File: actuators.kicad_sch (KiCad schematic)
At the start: 23 parts, among them U2 DRV8871 H-мост, U3 DRV8871 H-мост, U4 DRV8871 H-мост, U5 DRV8871 H-мост

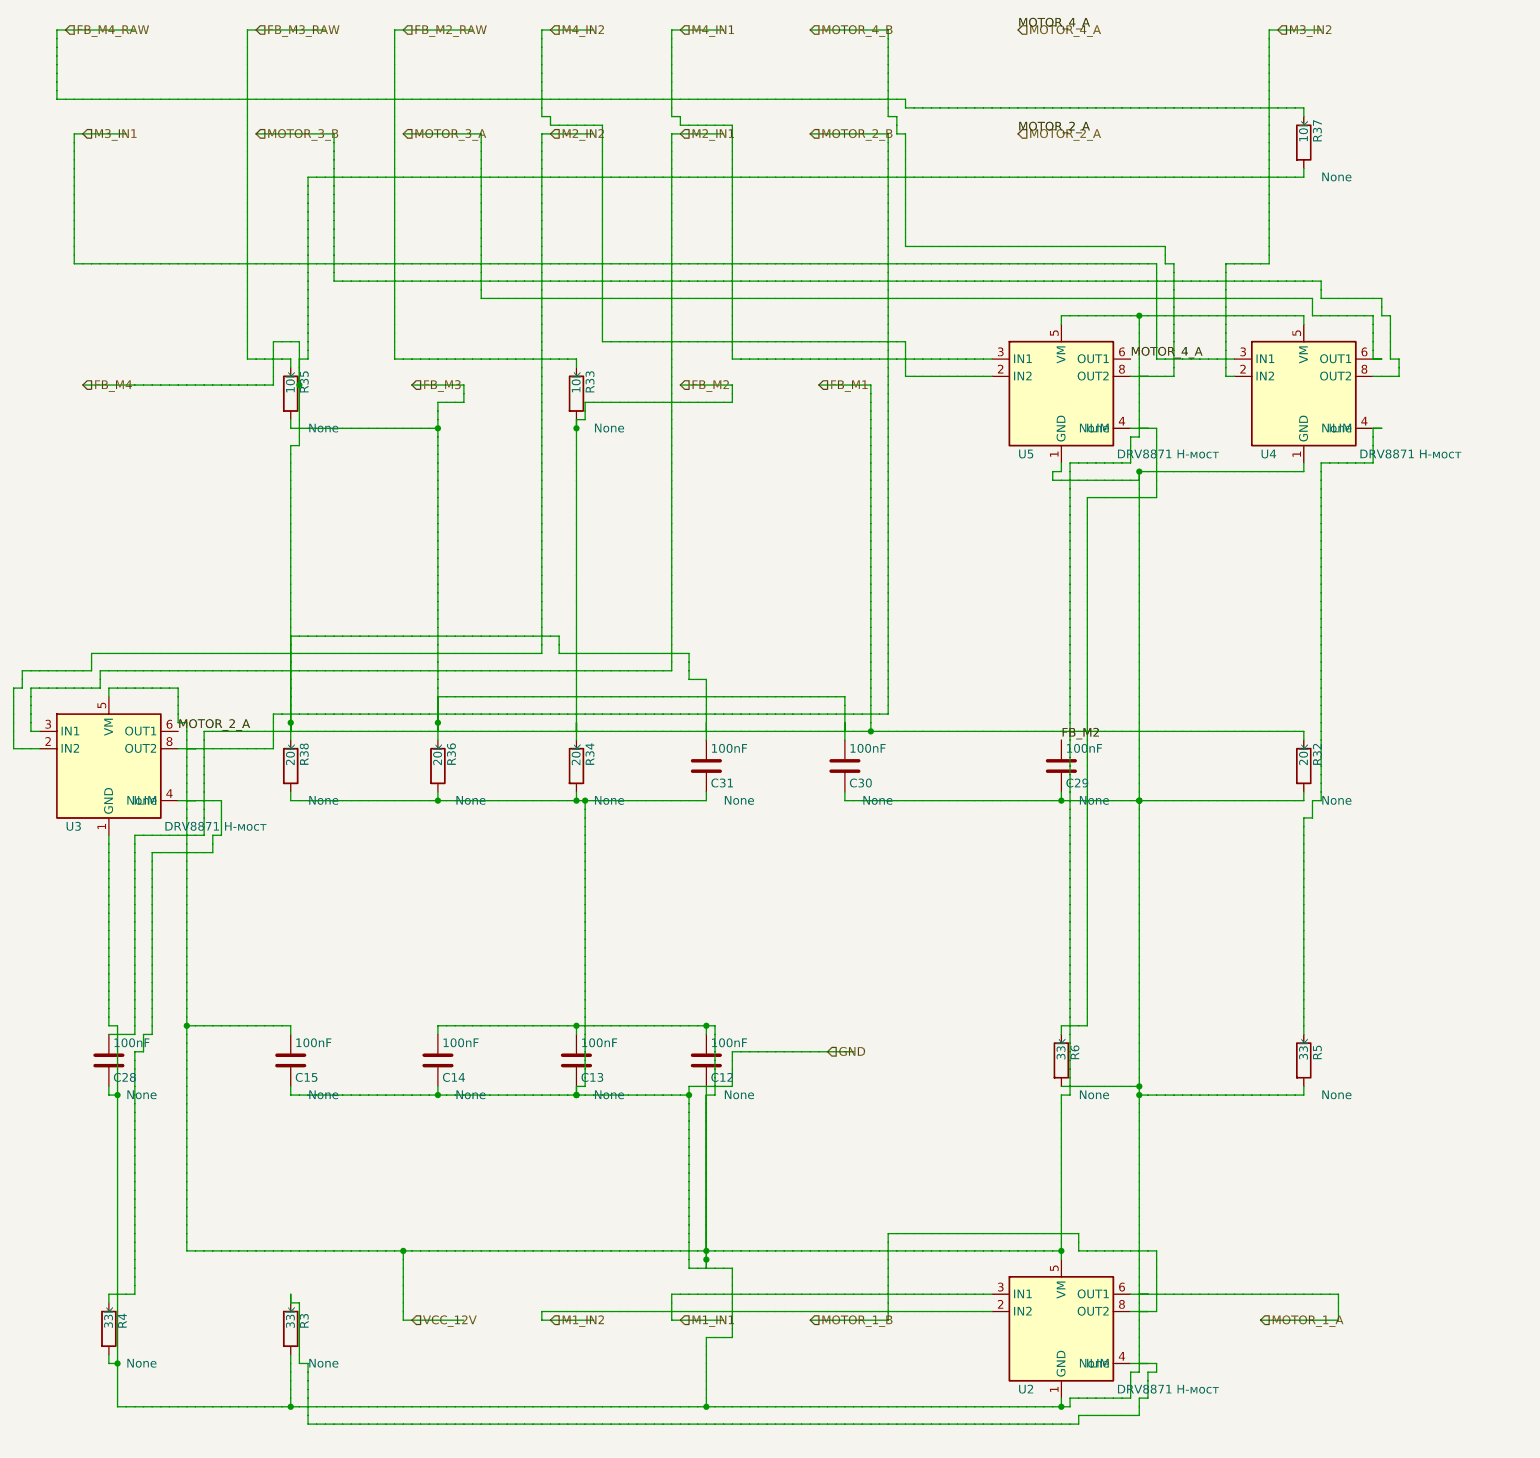
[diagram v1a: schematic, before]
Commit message: fix router map cell no more mark for pins
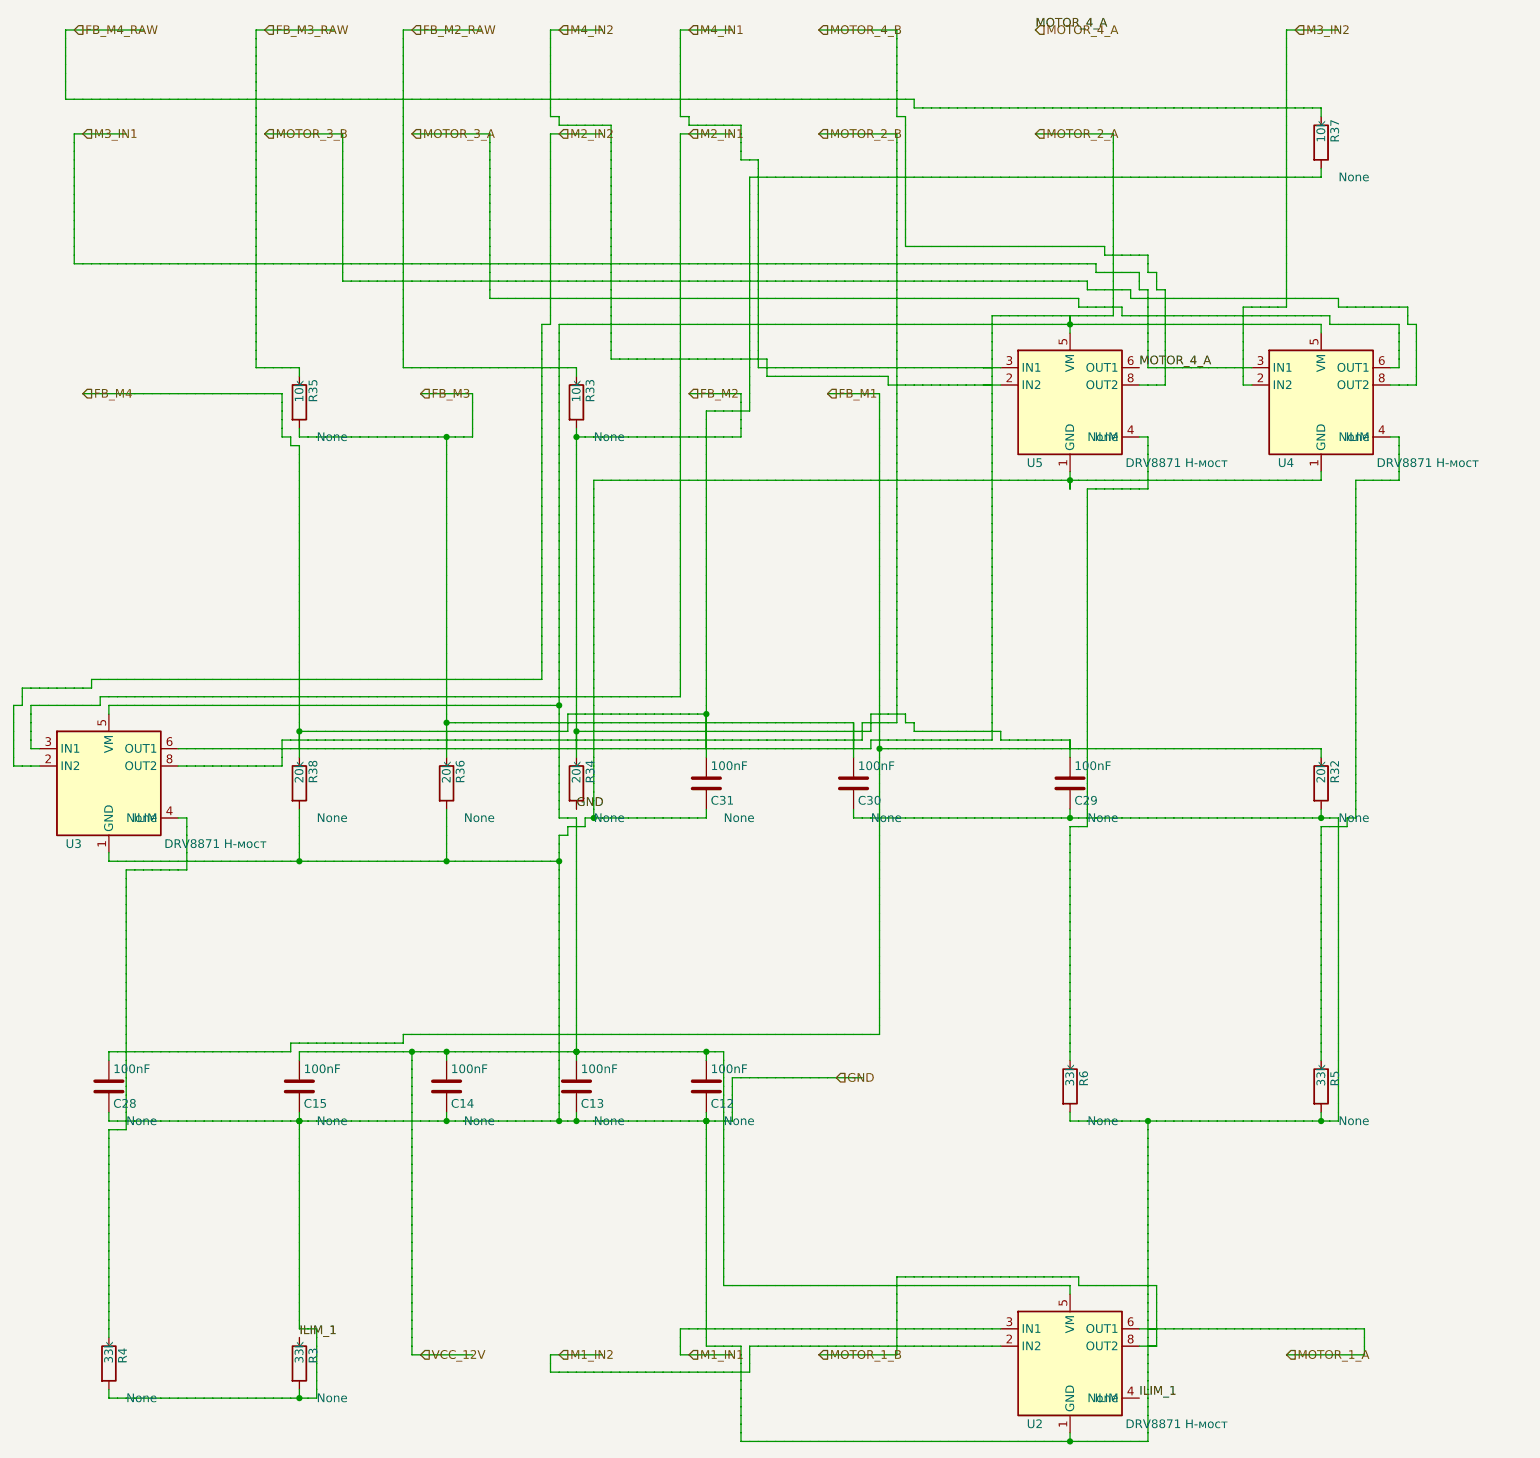
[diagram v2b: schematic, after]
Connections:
- net MOTOR_2_A is gone; now on net FB_M1: U3.6 (OUT1)
- net FB_M1: now also R5.1, U4.4 (ILIM); no longer R3.1, U2.4 (ILIM)
- new net ILIM_1: R3.1, U2.4 (ILIM)
